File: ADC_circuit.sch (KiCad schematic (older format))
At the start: 30 parts, among them J7 RF_Shield_One_Piece, U301 LT6600IS8, U302 LTC2386-18, U303 SN65LVDS1050PW

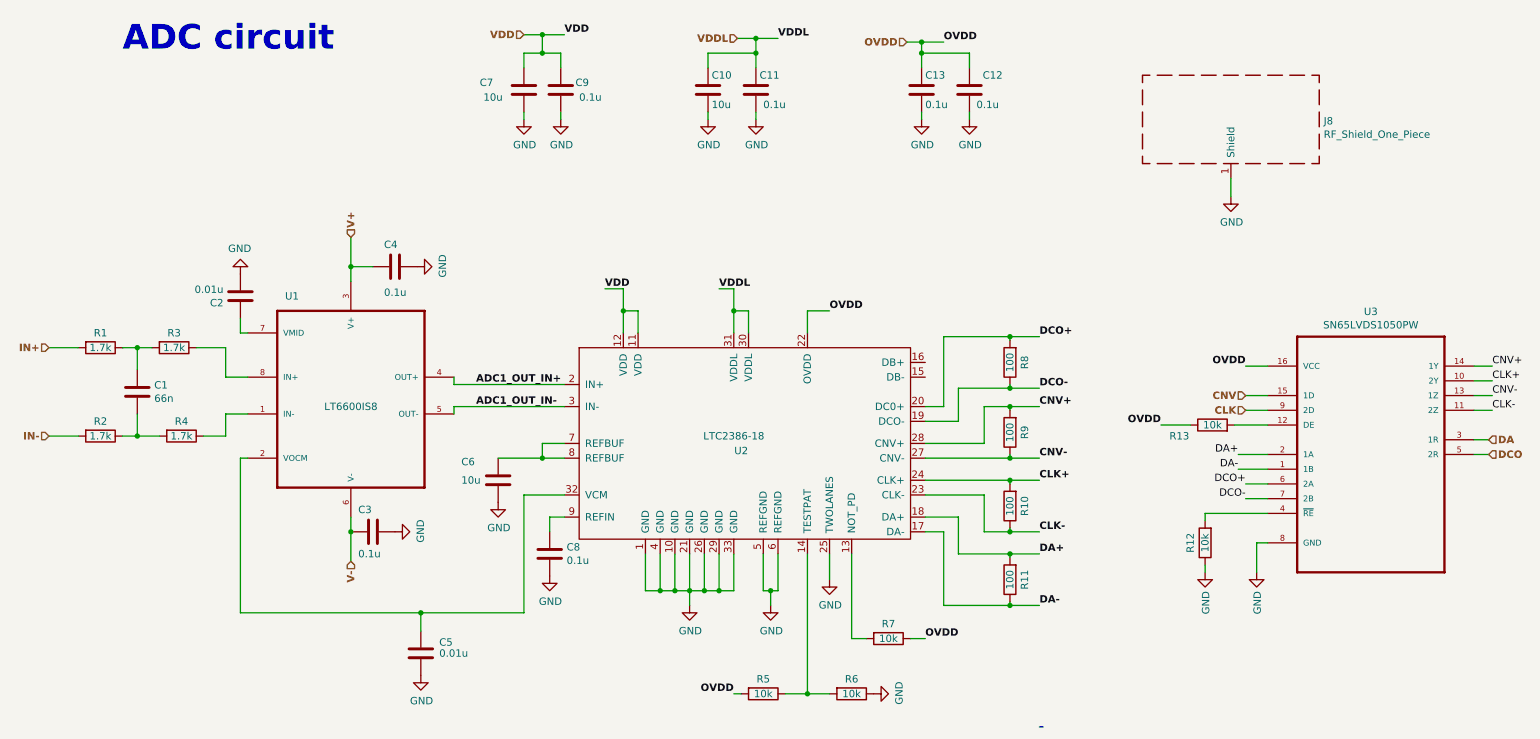
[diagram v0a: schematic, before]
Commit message: initial placement of all ADC/DAC blocks and added FPGA
Signed-off-by: Alexis Jeandet <alexis.jeandet@member.fsf.org>
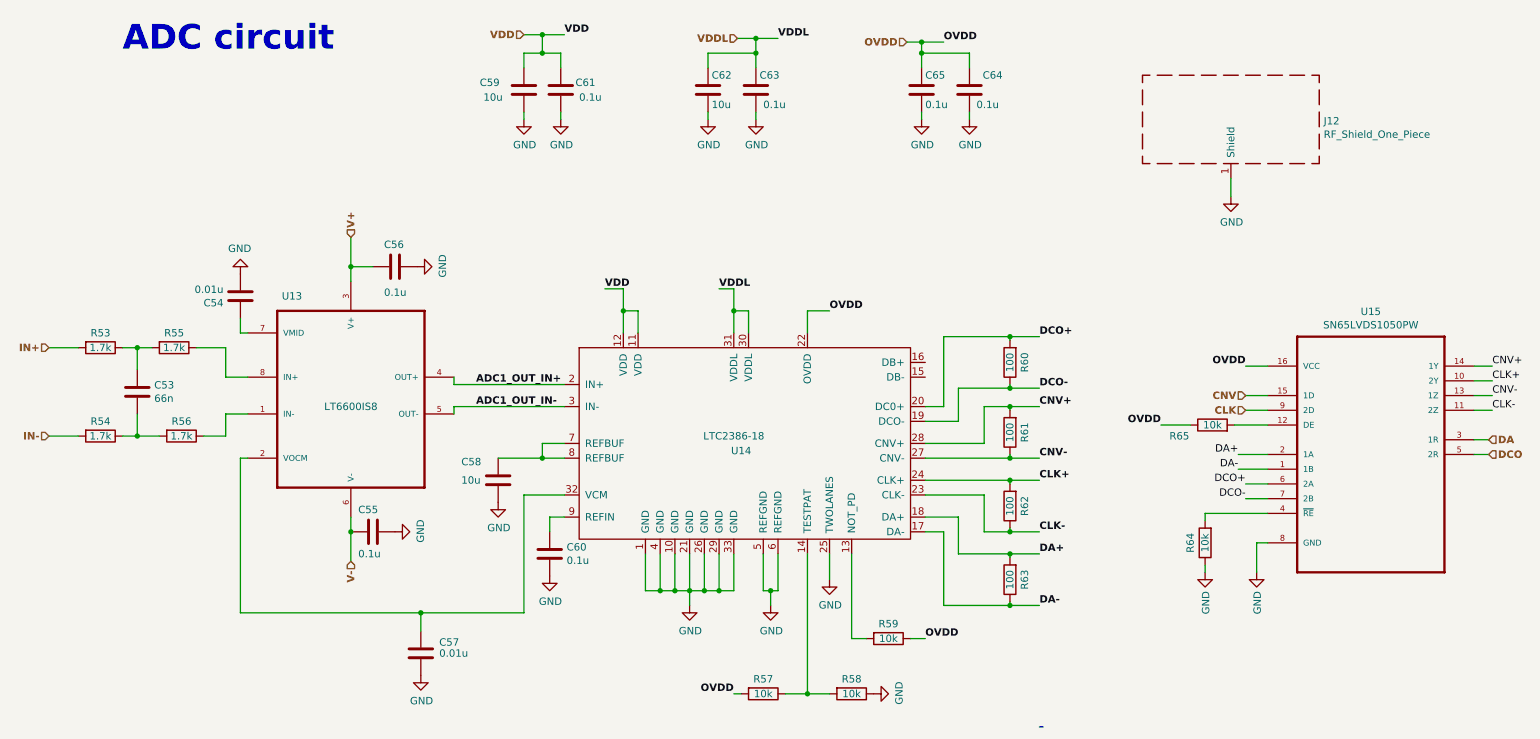
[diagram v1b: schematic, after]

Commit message: Layout done for ADC + LVDS and DAC -> FPGA
Signed-off-by: Alexis Jeandet <alexis.jeandet@member.fsf.org>
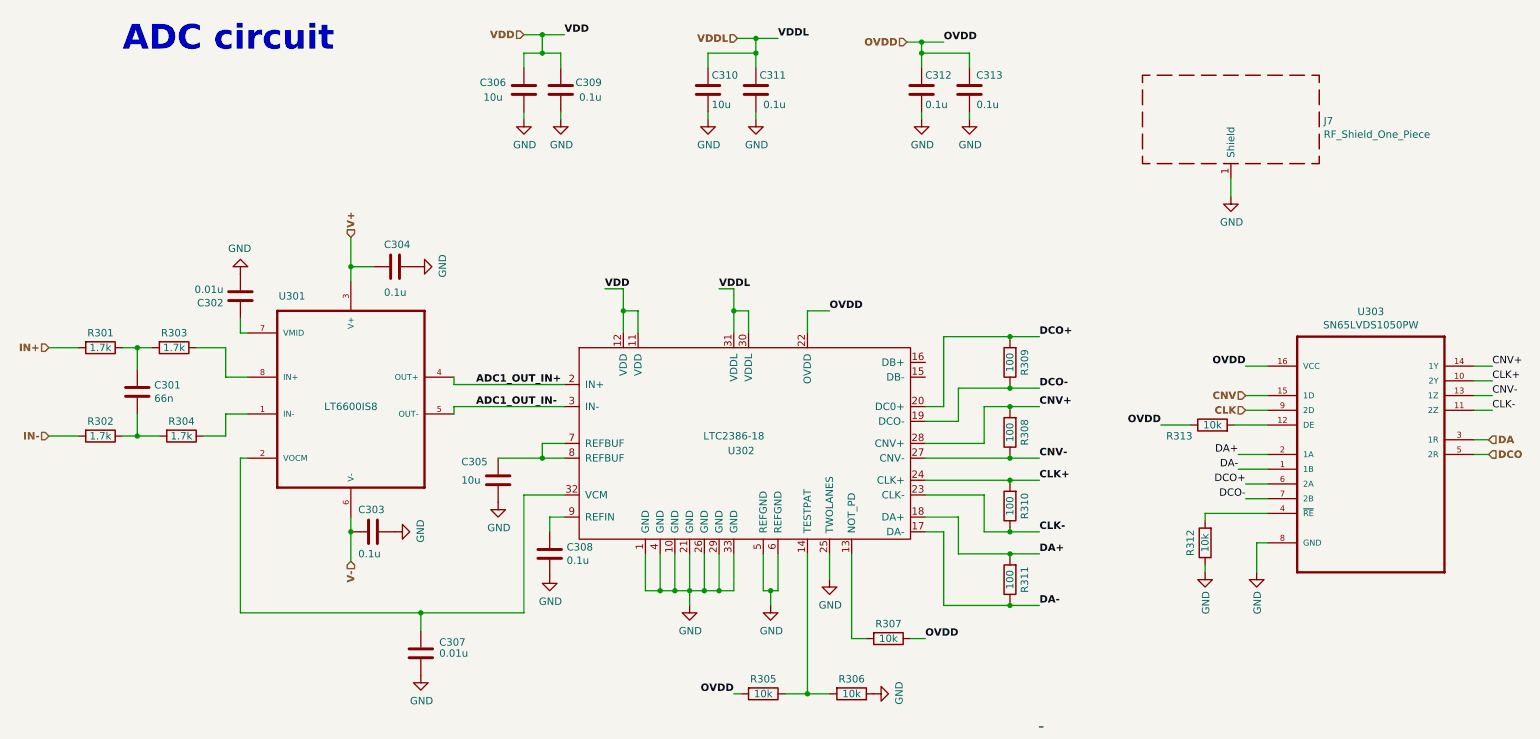
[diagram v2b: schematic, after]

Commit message: Added #3.3V and #1.2V supply, completed ADC to USB board layout, added DAC FPGA to USB board bus.
Signed-off-by: Alexis Jeandet <alexis.jeandet@member.fsf.org>
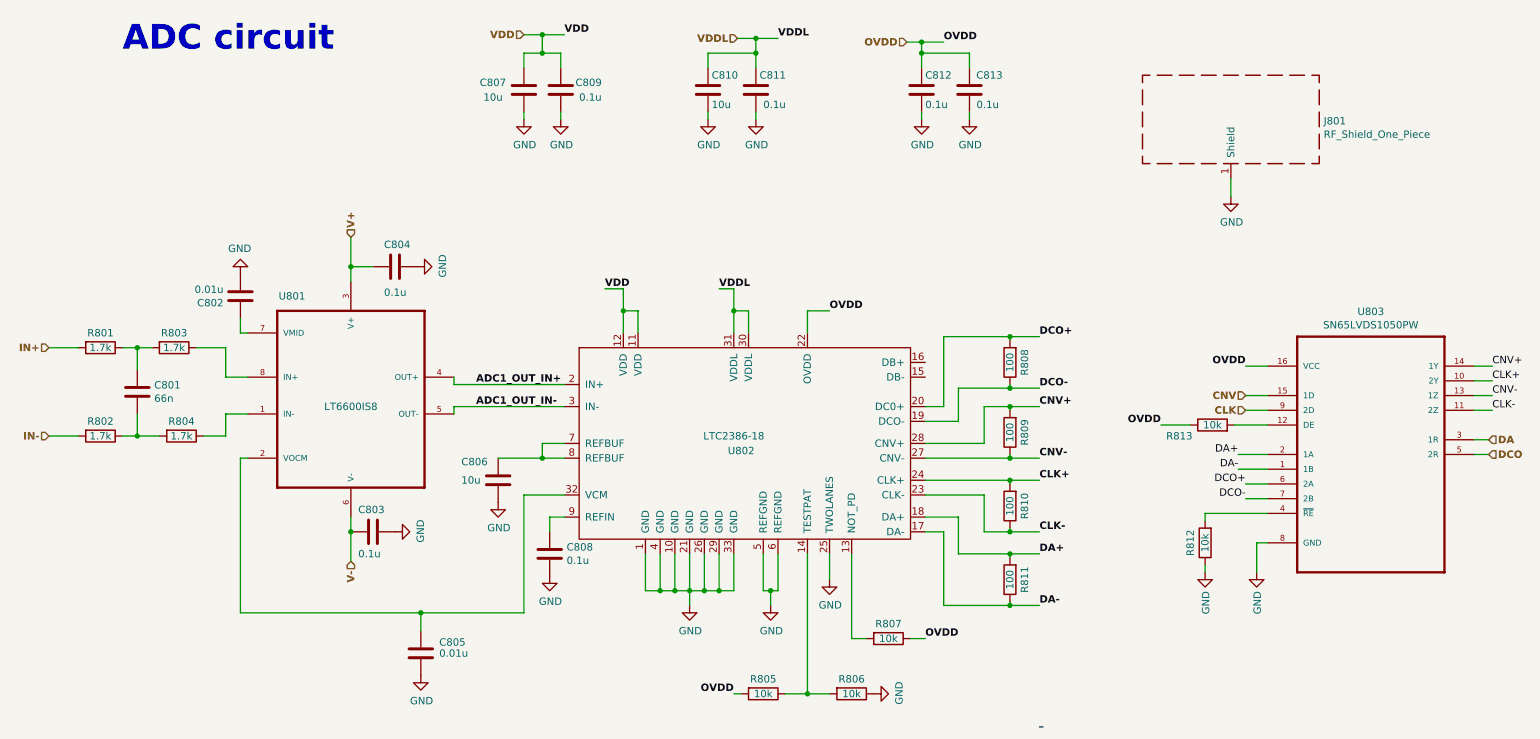
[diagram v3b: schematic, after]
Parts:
- renumbered C307 to C305, C305 to C306, C306 to C307, J7 to J301, R309 to R308, R308 to R309

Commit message: Desing as ordered for V1.0
Signed-off-by: Alexis Jeandet <alexis.jeandet@member.fsf.org>
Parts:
- U302: footprint Package_DFN_QFN:QFN-32-1EP_5x5mm_P0.5mm_EP3.45x3.45mm_ThermalVias -> Package_DFN_QFN:QFN-32-1EP_5x5mm_P0.5mm_EP3.45x3.45mm
